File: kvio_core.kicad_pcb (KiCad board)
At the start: 6 copper layers, 60 x 41 mm, 196 parts, among them J1001 16-pin_FFC_(SFV16R), J1101 16-pin_FFC_(SFV16R), J1301 USB3_B_Micro, J401 16-pin_FFC_(SFV16R), J501 16-pin_FFC_(SFV16R), J601 16-pin_FFC_(SFV16R), J701 16-pin_FFC_(SFV16R), J801 16-pin_FFC_(SFV16R), J901 16-pin_FFC_(SFV16R), U1001 EMI8143, U101 XC7A100T-CSG324, U1101 EMI8143, U1201 DDR3-16x, U1301 FT601Q, U1302 EMI8143, U201 FAN53541, U202 FAN53541, U203 FAN53541, U204 FAN53541, U401 EMI8143, U501 EMI8143, U601 EMI8143, U701 EMI8143, U801 EMI8143, U901 EMI8143, Y1301 Crystal_GND24_Small

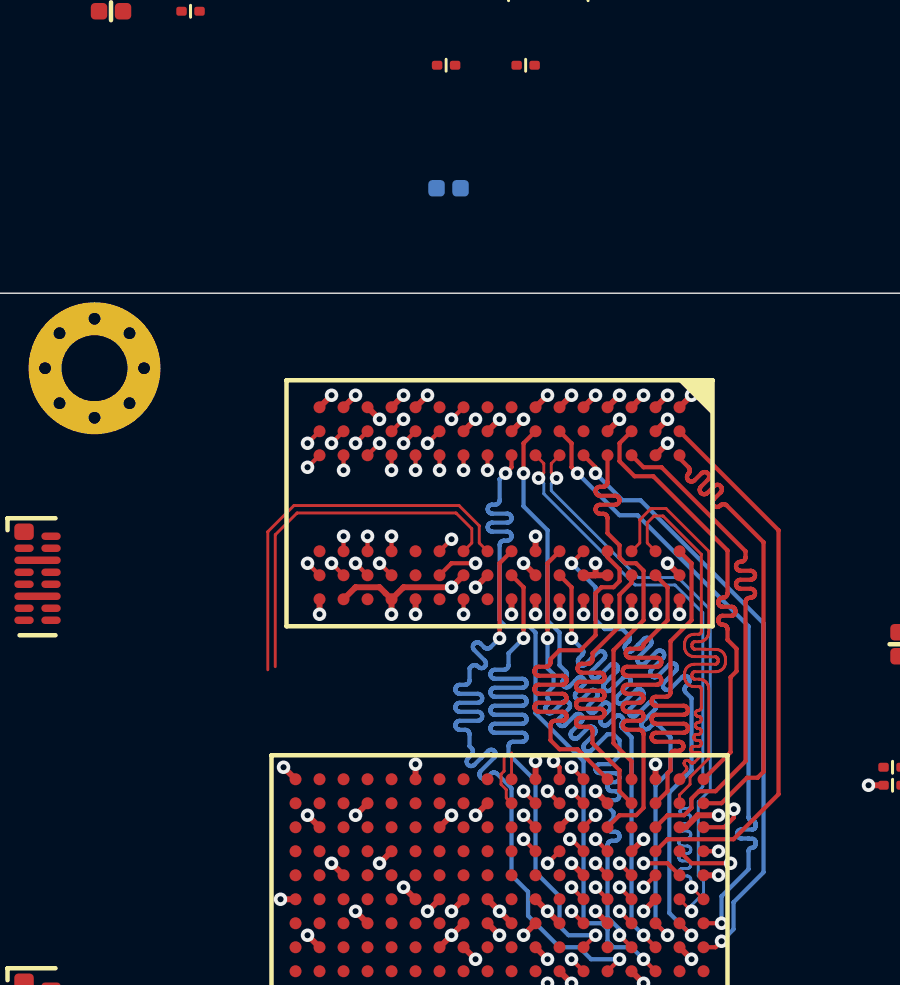
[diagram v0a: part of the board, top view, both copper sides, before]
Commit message: Updates to length matching and added GND plane for DDR3
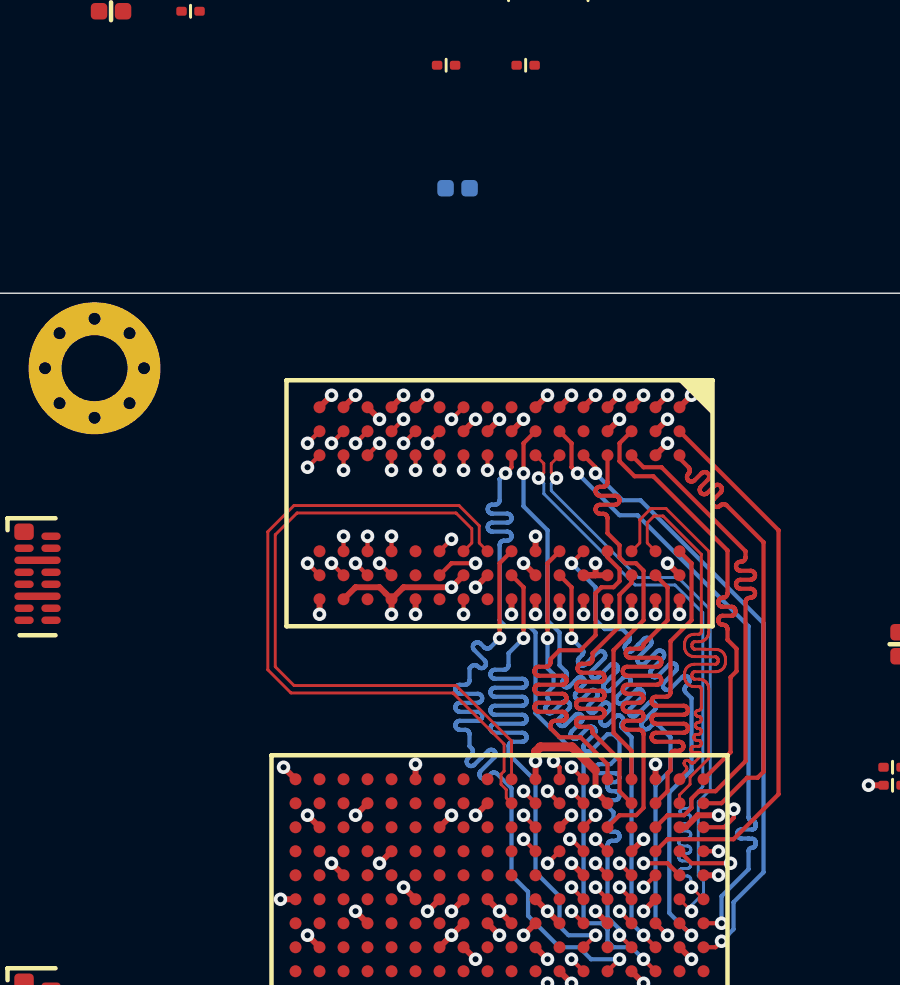
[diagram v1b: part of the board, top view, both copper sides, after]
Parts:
- moved C217 0.30 mm to (183.6, 85.5)
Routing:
- net /DDR Memory/CK_N: track 13.2 -> 22.5 mm
- net /DDR Memory/CK_P: track 15.0 -> 24.3 mm
- net /DDR Memory/DDR3_VDD: track 17.7 -> 21.2 mm
- added copper zone on GND_PWR2, net GND

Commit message: More design
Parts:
- removed C302: 0.1u, passive:C_0201
- added C283: 0.1u, passive:C_0201, F.Cu at (152.0, 111.5)
- added C284: 0.1u, passive:C_0201, F.Cu at (154.2, 111.5)
- added R301: 33, passive:R_0402, F.Cu at (144.4, 111.6)
- added R302: 470, passive:R_0402, F.Cu at (144.4, 113.5)
- added U301: MX25L3233F, Package_SON:WSON-8-1EP_6x5mm_P1.27mm_EP3.4x4.3mm, F.Cu at (139.5, 113.0)
- U101: value XC7A100T-CSG324 -> xc7a100t-csg324
- moved C301 50.6 mm to (141.5, 110.0)
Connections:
- net /VCCO_14 renamed /Power/VCCO_14
- net /VCCO_15 renamed /Power/VCCO_15
- net /VCCO_16 renamed /Power/VCCO_16
- C201 pad 1: /VCCO_34 -> /Power/VCCO_34
- C202 pad 1: /VCCO_35 -> /Power/VCCO_35
- C205 pad 1: /VCCO_34 -> /Power/VCCO_34
- C206 pad 1: /VCCO_35 -> /Power/VCCO_35
- C210 pad 1: /VCCO_34 -> /Power/VCCO_34
- C211 pad 1: /VCCO_35 -> /Power/VCCO_35
- C215 pad 1: /VCCO_34 -> /Power/VCCO_34
- C216 pad 1: /VCCO_35 -> /Power/VCCO_35
- C220 pad 1: /VCCO_34 -> /Power/VCCO_34
- C221 pad 1: /VCCO_35 -> /Power/VCCO_35
- C226 pad 1: /VCCO_34 -> /Power/VCCO_34
- C227 pad 1: /VCCO_35 -> /Power/VCCO_35
- C232 pad 1: /VCCO_34 -> /Power/VCCO_34
- C233 pad 1: /VCCO_35 -> /Power/VCCO_35
- C240 pad 1: /VCCO_34 -> /Power/VCCO_34
- C241 pad 1: /VCCO_35 -> /Power/VCCO_35
- C248 pad 1: /VCCO_34 -> /Power/VCCO_34
- C249 pad 1: /VCCO_35 -> /Power/VCCO_35
- C256 pad 1: /VCCO_34 -> /Power/VCCO_34
- C257 pad 1: /VCCO_35 -> /Power/VCCO_35
- C301 pad 1: /Config/VCCO_0 -> GND
- C301 pad 2: GND -> /Config/3V3
- U101 pad A7: /USB3 Interface/3V3 -> /Power/VCCO_35
- U101 pad C3: /USB3 Interface/3V3 -> /Power/VCCO_35
- U101 pad D6: /USB3 Interface/3V3 -> /Power/VCCO_35
- U101 pad F2: /USB3 Interface/3V3 -> /Power/VCCO_35
- U101 pad G5: /USB3 Interface/3V3 -> /Power/VCCO_35
- U101 pad J1: /USB3 Interface/3V3 -> /Power/VCCO_35
- U101 pad K4: /DDR Memory/DDR3_VDD -> /Power/VCCO_34
- U101 pad N3: /DDR Memory/DDR3_VDD -> /Power/VCCO_34
- U101 pad P6: /DDR Memory/DDR3_VDD -> /Power/VCCO_34
- U101 pad R9: /Config/VCCO_0 -> /Power/VCCO_0
- U101 pad T2: /DDR Memory/DDR3_VDD -> /Power/VCCO_34
- U101 pad U5: /DDR Memory/DDR3_VDD -> /Power/VCCO_34
- U101 pad V8: /DDR Memory/DDR3_VDD -> /Power/VCCO_34
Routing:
- net /Power/VCCO_34: track 0.00 -> 7.84 mm, vias 0 -> 6
- net /DDR Memory/DDR3_VDD: track 21.2 -> 13.3 mm, vias 23 -> 17

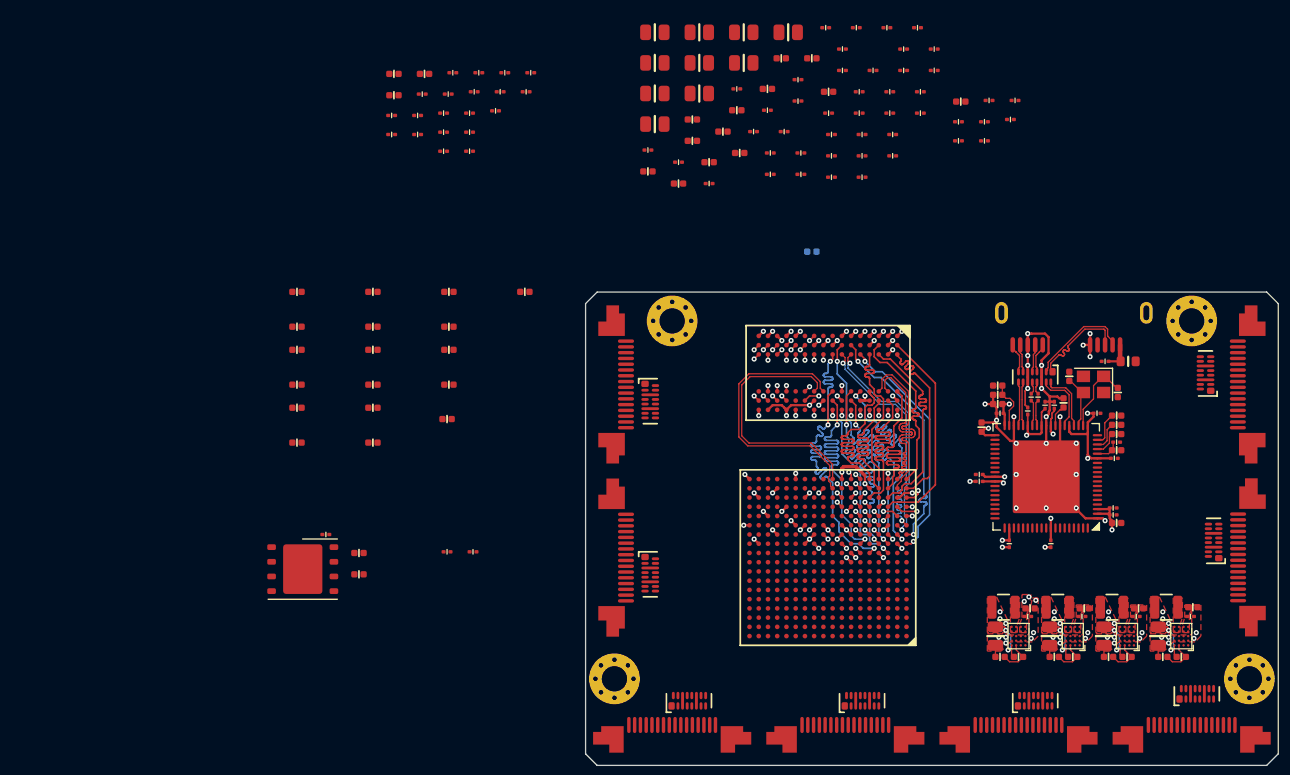
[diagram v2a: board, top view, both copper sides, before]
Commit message: More additions, DDR3 caps placed
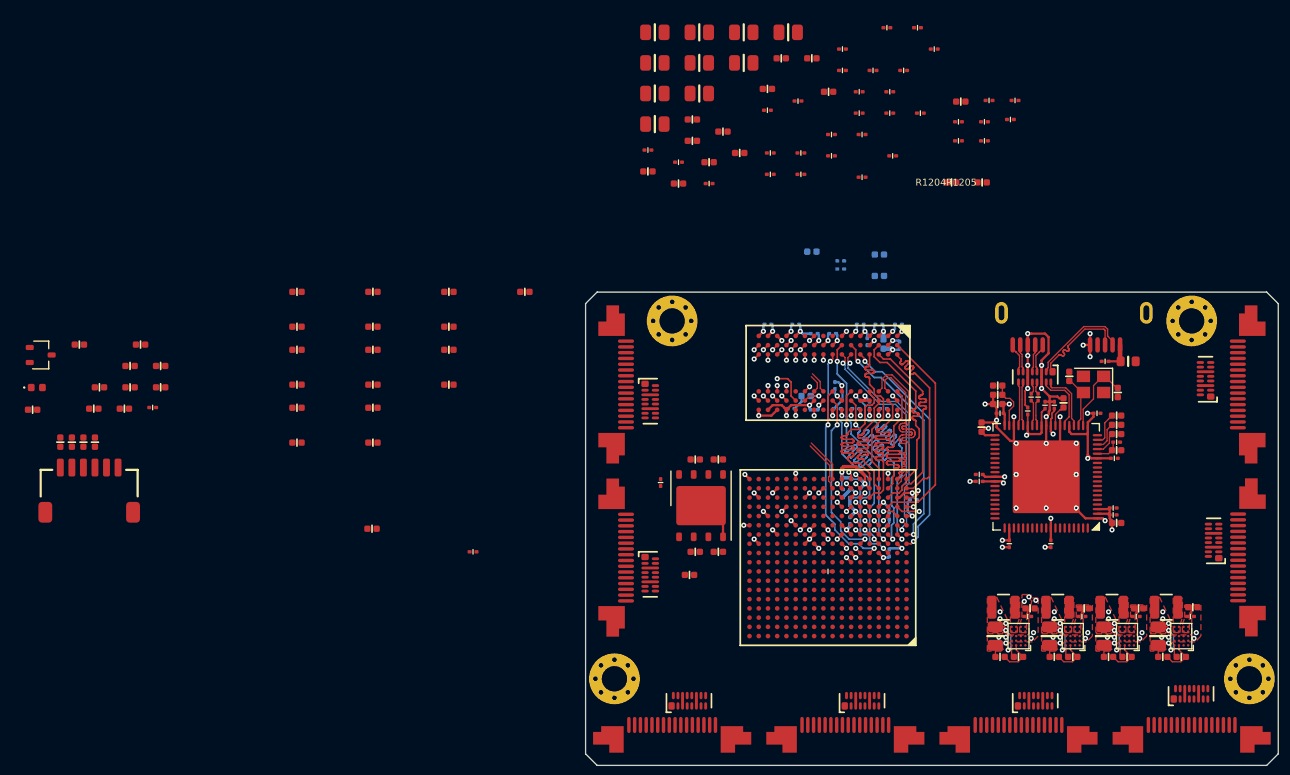
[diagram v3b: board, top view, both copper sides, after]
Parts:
- removed C1205, C1209, C242, C250, C256, C257, C258, C259, C260, C283: 0.1u, passive:C_0201
- removed C222: 4.7u, passive:C_0402
- added C285: 0.1u, passive:C_0201, F.Cu at (185.0, 113.2)
- added C302: 0.1u, passive:C_0201, F.Cu at (126.5, 99.0)
- added D301: GREEN, LED_SMD:LED_0402_1005Metric, F.Cu at (116.5, 97.3)
- added J301: Conn_01x06_Male, connectors:jst-sh-hor-6, F.Cu at (121.0, 106.0)
- added R1204: 80, passive:R_0402, F.Cu at (195.7, 79.5)
- added R1205: 4.7k, passive:R_0402, F.Cu at (198.3, 79.5)
- added R303: 470, passive:R_0402, F.Cu at (127.2, 95.4)
- added R304: 1k, passive:R_0402, F.Cu at (124.0, 99.1)
- added R305: 1k, passive:R_0402, F.Cu at (124.5, 97.2)
- added R306: 1k, passive:R_0402, F.Cu at (124.5, 95.4)
- added R307: 10k, passive:R_0402, F.Cu at (121.4, 99.1)
- added R308: 1k, passive:R_0402, F.Cu at (121.9, 97.2)
- added R309: 1k, passive:R_0402, F.Cu at (127.2, 97.2)
- added R310: 1k, passive:R_0402, F.Cu at (125.5, 93.5)
- added R311: 33, passive:R_0402, F.Cu at (175.5, 103.5)
- added R312: 33, passive:R_0402, F.Cu at (173.5, 111.5)
- added R313: 33, passive:R_0402, F.Cu at (175.5, 111.5)
- added R314: 33, passive:R_0402, F.Cu at (173.5, 103.5)
- added R315: 10k, passive:R_0402, F.Cu at (116.1, 99.2)
- added R316: 10k, passive:R_0402, F.Cu at (120.2, 93.5)
- added R317: 33, passive:R_0402, F.Cu at (118.5, 102.0)
- added R318: 33, passive:R_0402, F.Cu at (119.5, 102.0)
- added R319: 33, passive:R_0402, F.Cu at (120.5, 102.0)
- added R320: 33, passive:R_0402, F.Cu at (121.5, 102.0)
- added U302: MAX809, sot:SOT-323, F.Cu at (116.8, 94.5)
- C1201, C1202, C1203, C1204, C1206, C1207, C1208, C1210, C1211, C1212, C1213, C1214, C1215, C1216, C1217, C1218, C1219, C1220, C1221, C215, C220, C226, C232, C240, C248, R1201, R1202, R1203: moved to B.Cu
- U1201: value DDR3-16x -> MT41J128M16JT-125:K
- moved C1203 46.1 mm to (189.8, 93.5), turned to 270 degrees
- moved C1212 45.8 mm to (191.1, 91.8), turned to 180 degrees
- moved R1202 45.5 mm to (189.4, 87.6)
- moved R1201 44.3 mm to (189.4, 85.8)
- moved C1213 43.6 mm to (191.2, 93.6), turned to 90 degrees
- moved C1204 42.9 mm to (189.4, 91.8), turned to 180 degrees
- moved C215 42.7 mm to (186.9, 108.8), turned to 270 degrees
- moved C220 42.7 mm to (190.3, 108.4), turned to 90 degrees
- moved C1210 42.6 mm to (185.8, 99.1)
- moved C1219 42.4 mm to (189.8, 99.1), turned to 180 degrees
- moved C1214 42.1 mm to (187.4, 99.1), turned to 180 degrees
- moved C1217 41.1 mm to (188.6, 98.8), turned to 270 degrees
- moved C1202 40.9 mm to (186.1, 86.3)
- moved C1206 40.6 mm to (185.4, 92.6), turned to 180 degrees
- moved C1216 40.2 mm to (188.4, 93.3), turned to 90 degrees
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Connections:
- C201 pad 1: /Power/VCCO_34 -> +1V5
- C202 pad 1: /Power/VCCO_35 -> +3V3
- C203 pad 1: /Power/VCCO_15 -> +3V3
- C204 pad 1: /Power/VCCO_14 -> +3V3
- C205 pad 1: /Power/VCCO_34 -> +1V5
- C206 pad 1: /Power/VCCO_35 -> +3V3
- C207 pad 1: /Power/VCCO_15 -> +3V3
- C208 pad 1: /Power/VCCO_14 -> +3V3
- C209 pad 1: /Power/VCCINT -> +1V0
- C210 pad 1: /Power/VCCO_34 -> +1V5
- C211 pad 1: /Power/VCCO_35 -> +3V3
- C212 pad 1: /Power/VCCO_15 -> +3V3
- C213 pad 1: /Power/VCCO_14 -> +3V3
- C214 pad 1: /Power/VCCINT -> +1V0
- C215 pad 1: /Power/VCCO_34 -> +1V5
- C216 pad 1: /Power/VCCO_35 -> +3V3
- C217 pad 1: /Power/VCCO_15 -> +3V3
- C218 pad 1: /Power/VCCO_14 -> +3V3
- C219 pad 1: /Power/VCCINT -> +1V0
- C220 pad 1: /Power/VCCO_34 -> +1V5
- C221 pad 1: /Power/VCCO_35 -> +3V3
- C223 pad 1: /Power/VCCO_15 -> +3V3
- C224 pad 1: /Power/VCCO_14 -> +3V3
- C225 pad 1: /Power/VCCINT -> +1V0
- C226 pad 1: /Power/VCCO_34 -> +1V5
- C227 pad 1: /Power/VCCO_35 -> +3V3
- C228 pad 1: /Power/VCCO_16 -> +3V3
- C229 pad 1: /Power/VCCO_15 -> +3V3
- C230 pad 1: /Power/VCCO_14 -> +3V3
- C231 pad 1: /Power/VCCINT -> +1V0
- C232 pad 1: /Power/VCCO_34 -> +1V5
- C233 pad 1: /Power/VCCO_35 -> +3V3
- C234 pad 1: /Power/VCCO_16 -> +3V3
- C235 pad 1: /Power/VCCO_15 -> +3V3
- C236 pad 1: /Power/VCCO_14 -> +3V3
- C237 pad 1: /Power/VCCINT -> +1V0
- C238 pad 1: /Power/VCCAUX -> +1V8
- C239 pad 1: /Power/VCCBRAM -> +1V0
- C240 pad 1: /Power/VCCO_34 -> +1V5
- C241 pad 1: /Power/VCCO_35 -> +3V3
- C243 pad 1: /Power/VCCO_15 -> +3V3
- C244 pad 1: /Power/VCCO_14 -> +3V3
- C245 pad 1: /Power/VCCINT -> +1V0
- C246 pad 1: /Power/VCCAUX -> +1V8
- C247 pad 1: /Power/VCCAUX -> +1V8
- C248 pad 1: /Power/VCCO_34 -> +1V5
- C249 pad 1: /Power/VCCO_35 -> +3V3
- C251 pad 1: /Power/VCCO_15 -> +3V3
- C252 pad 1: /Power/VCCO_14 -> +3V3
- C253 pad 1: /Power/VCCINT -> +1V0
- C254 pad 1: /Power/VCCAUX -> +1V8
- C255 pad 1: /Power/VCCBRAM -> +1V0
- C261 pad 1: /Power/VCCINT -> +1V0
- C262 pad 1: /Power/VCCAUX -> +1V8
- C263 pad 1: /Power/VCCBRAM -> +1V0
- C264 pad 1: /Power/VCCAUX -> +1V8
- C265 pad 1: /Power/VCCAUX -> +1V8
- C266 pad 1: /Power/VCCINT -> +1V0
- C267 pad 1: /Power/VCCINT -> +1V0
- C268 pad 1: /Power/VCCINT -> +1V0
- C269 pad 1: /Power/VCCINT -> +1V0
- C270 pad 1: /Power/VCCINT -> +1V0
- C273 pad 1: /Power/3V3 -> +3V3
- C276 pad 1: /Power/1V8 -> +1V8
- C279 pad 1: /Power/1V35 -> +1V5
- C282 pad 1: /Power/1V0 -> +1V0
- C284 pad 1: /Power/VCCO_0 -> +3V3
- FB201 pad 1: Net-(FB201-Pad1) -> /Power/VCCADC
- FB201 pad 2: Net-(FB201-Pad2) -> +1V8
- L201 pad 2: /Power/3V3 -> +3V3
- L202 pad 2: /Power/1V8 -> +1V8
- L203 pad 2: /Power/1V35 -> +1V5
- L204 pad 2: /Power/1V0 -> +1V0
- R201 pad 1: /Power/3V3 -> +3V3
- R203 pad 1: /Power/1V8 -> +1V8
- R205 pad 1: /Power/1V35 -> +1V5
- R207 pad 1: /Power/1V0 -> +1V0
- R301 pad 1: Net-(R301-Pad1) -> /Config/CFG_CLK
- R302 pad 1: Net-(D301-Pad2) -> /Config/CFG_DONE
- U101 pad A17: /Power/VCCO_15 -> +3V3
- U101 pad A7: /Power/VCCO_35 -> +3V3
- U101 pad B10: /Power/VCCO_16 -> +3V3
- U101 pad C13: /Power/VCCO_15 -> +3V3
- U101 pad C3: /Power/VCCO_35 -> +3V3
- U101 pad D16: /Power/VCCO_15 -> +3V3
- U101 pad D6: /Power/VCCO_35 -> +3V3
- U101 pad E10: Net-(U101-PadE10) -> /Config/TCK
- U101 pad E11: Net-(U101-PadE11) -> /Config/TDI
- U101 pad E12: Net-(U101-PadE12) -> /Config/TMS
- U101 pad E13: Net-(U101-PadE13) -> /Config/TDO
- U101 pad E8: /Power/VCCBAT -> +1V8
- U101 pad E9: Net-(U101-PadE9) -> Net-(R301-Pad2)
- U101 pad F10: /Power/VCCBRAM -> +1V0
- U101 pad F12: /Power/VCCAUX -> +1V8
- U101 pad F2: /Power/VCCO_35 -> +3V3
- U101 pad F8: /Power/VCCINT -> +1V0
- U101 pad G11: /Power/VCCBRAM -> +1V0
- U101 pad G15: /Power/VCCO_15 -> +3V3
- U101 pad G5: /Power/VCCO_35 -> +3V3
- U101 pad G7: /Power/VCCINT -> +1V0
- U101 pad G9: /Power/VCCINT -> +1V0
- U101 pad H12: /Power/VCCAUX -> +1V8
- U101 pad H18: /Power/VCCO_15 -> +3V3
- U101 pad H8: /Power/VCCINT -> +1V0
- U101 pad H9: /Power/GNDADC -> GND
- U101 pad J1: /Power/VCCO_35 -> +3V3
- U101 pad J10: Net-(U101-PadJ10) -> GND
- U101 pad J11: /Power/VCCINT -> +1V0
- U101 pad J7: /Power/VCCINT -> +1V0
- U101 pad J9: Net-(U101-PadJ9) -> GND
- U101 pad K10: Net-(U101-PadK10) -> GND
- U101 pad K12: /Power/VCCAUX -> +1V8
- U101 pad K14: /Power/VCCO_15 -> +3V3
- U101 pad K17: Net-(U101-PadK17) -> /Config/CFG_D0
- U101 pad K18: Net-(U101-PadK18) -> /Config/CFG_D1
- U101 pad K4: /Power/VCCO_34 -> +1V5
- U101 pad K8: /Power/VCCINT -> +1V0
- U101 pad K9: Net-(U101-PadK9) -> GND
- U101 pad L10: Net-(U101-PadL10) -> GND
- U101 pad L11: /Power/VCCINT -> +1V0
- U101 pad L13: Net-(U101-PadL13) -> /Config/CFG_CS
- U101 pad L14: Net-(U101-PadL14) -> /Config/CFG_D2
- U101 pad L15: Net-(U101-PadL15) -> /Config/CFG_PUDC
- U101 pad L17: /Power/VCCO_14 -> +3V3
- U101 pad L7: /Power/VCCINT -> +1V0
- U101 pad L9: Net-(U101-PadL9) -> GND
- U101 pad M10: /Power/VCCINT -> +1V0
- U101 pad M12: /Power/VCCAUX -> +1V8
- U101 pad M14: Net-(U101-PadM14) -> /Config/CFG_D3
- U101 pad M8: /Power/VCCINT -> +1V0
- U101 pad N11: /Power/VCCINT -> +1V0
- U101 pad N13: /Power/VCCO_14 -> +3V3
- U101 pad N3: /Power/VCCO_34 -> +1V5
- U101 pad N7: /Power/VCCINT -> +1V0
- U101 pad N9: /Power/VCCINT -> +1V0
- U101 pad P10: Net-(U101-PadP10) -> /Config/CFG_DONE
- U101 pad P11: Net-(U101-PadP11) -> /Config/CFG_MODE2
- U101 pad P12: Net-(U101-PadP12) -> /Config/CFG_MODE0
- U101 pad P13: Net-(U101-PadP13) -> /Config/CFG_MODE1
- U101 pad P16: /Power/VCCO_14 -> +3V3
- U101 pad P6: /Power/VCCO_34 -> +1V5
- U101 pad P7: Net-(U101-PadP7) -> /Config/CFG_INIT_B
- U101 pad P8: Net-(U101-PadP8) -> /Config/3V3
- U101 pad P9: Net-(U101-PadP9) -> /Config/CFG_PROGRAM_B
- U101 pad R9: /Power/VCCO_0 -> +3V3
- U101 pad T12: /Power/VCCO_14 -> +3V3
- U101 pad T2: /Power/VCCO_34 -> +1V5
- U101 pad U15: /Power/VCCO_14 -> +3V3
- U101 pad U5: /Power/VCCO_34 -> +1V5
- U101 pad V18: /Power/VCCO_14 -> +3V3
- U101 pad V8: /Power/VCCO_34 -> +1V5
- U201 pad A4: /Power/3V3 -> +3V3
- U202 pad A4: /Power/1V8 -> +1V8
- U203 pad A4: /Power/1V35 -> +1V5
- U204 pad A4: /Power/1V0 -> +1V0
- U301 pad 1: Net-(U301-Pad1) -> /Config/CFG_CS
- U301 pad 6: Net-(U301-Pad6) -> /Config/CFG_CLK
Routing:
- net GND: track 72.2 -> 97.4 mm
- net +1V5: track 0.00 -> 22.4 mm, vias 0 -> 11
- net /DDR Memory/CK_P: track 24.3 -> 6.49 mm
- net /DDR Memory/CK_N: track 22.5 -> 5.50 mm
- net /DDR Memory/DDR3_VDD: track 13.3 -> 26.5 mm
- net /DDR Memory/DQ5: track 23.2 -> 15.0 mm
- net +3V3: track 0.00 -> 7.87 mm, vias 0 -> 11
- net /Power/VCCO_34: track 7.84 -> 0.00 mm, vias 6 -> 0
- net /DDR Memory/DQ7: track 25.0 -> 17.2 mm
- net /DDR Memory/A1: track 21.8 -> 14.4 mm
- net +1V0: track 0.00 -> 7.31 mm, vias 0 -> 10
- net /DDR Memory/LDQS_N: track 21.3 -> 15.4 mm
- net /Power/3V3: track 4.48 -> 0.00 mm, vias 5 -> 0
- net /Power/1V8: track 4.48 -> 0.00 mm, vias 5 -> 0
- net +1V8: track 0.00 -> 4.48 mm, vias 0 -> 5
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- added copper zone on F.Cu, net +1V0
- added copper zone on F.Cu, net +1V5
- added copper zone on F.Cu, net +1V8
- added copper zone on F.Cu, net +3V3
- removed copper zone on F.Cu, net /Power/1V0
- removed copper zone on F.Cu, net /Power/1V35
- removed copper zone on F.Cu, net /Power/1V8
- removed copper zone on F.Cu, net /Power/3V3
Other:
- net class Default: clearance 0.1 -> 0.0889
- net class power: clearance 0.1 -> 0.0889
- rule trace_clearance: 0.1 -> 0.0889

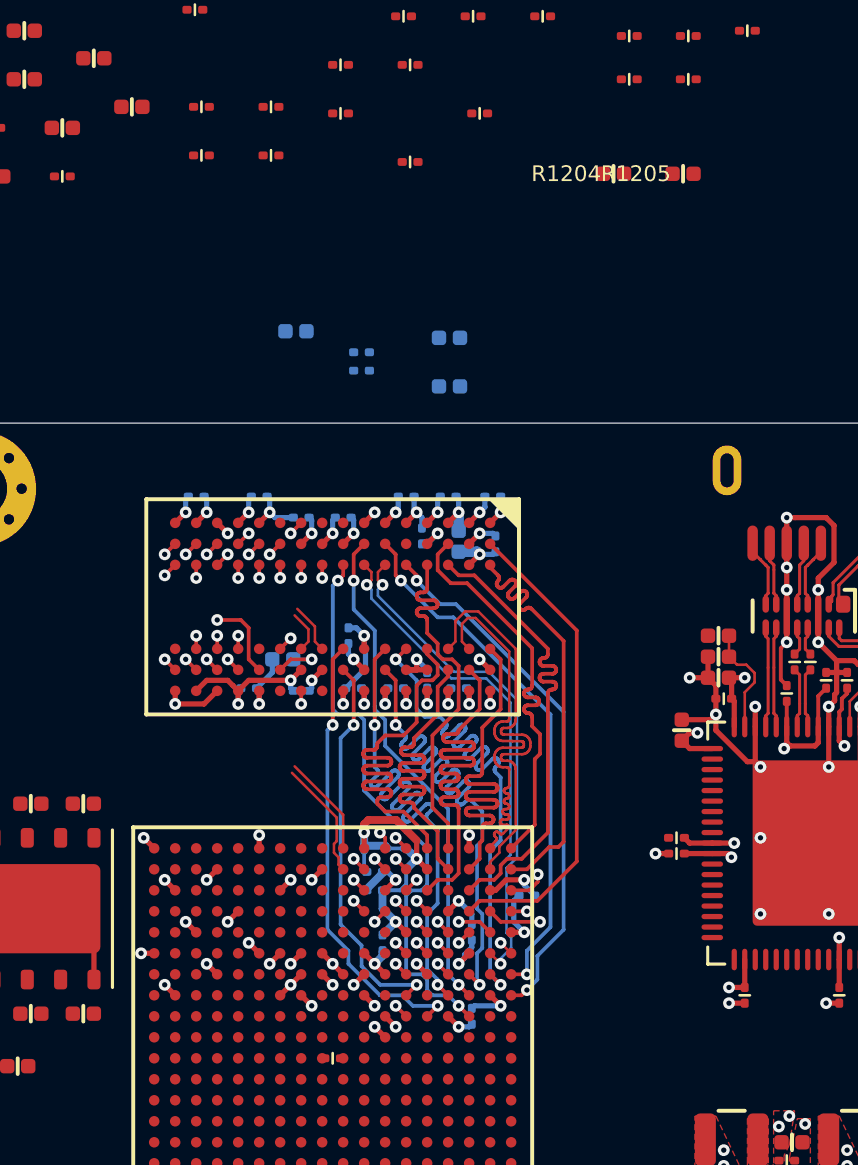
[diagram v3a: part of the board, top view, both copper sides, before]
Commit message: Fixing with DDR3, needs retuning
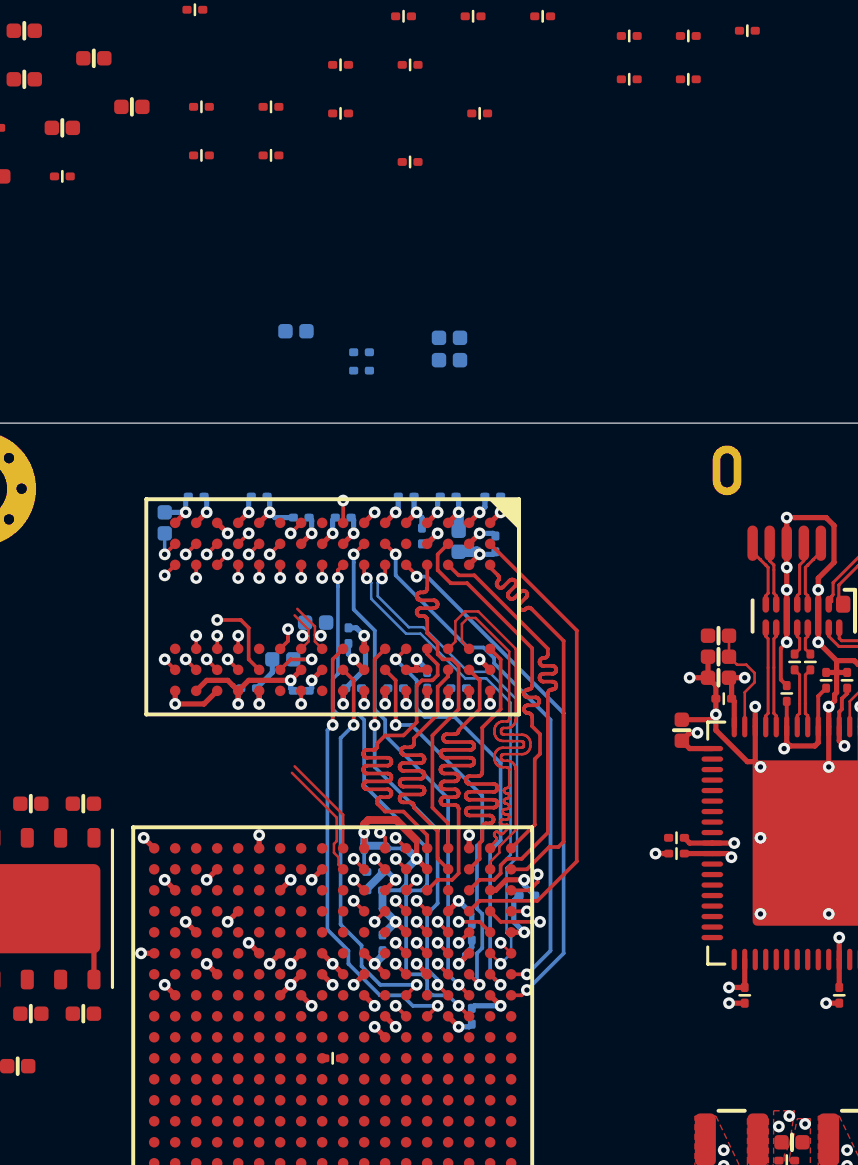
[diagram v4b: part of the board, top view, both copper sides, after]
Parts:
- R1204, R1205: moved to B.Cu
- moved R1205 23.8 mm to (178.6, 92.8), turned to 90 degrees
- moved R1204 20.5 mm to (184.3, 96.6), turned to 180 degrees
- moved R1202 1.00 mm to (189.4, 86.6)
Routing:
- net /DDR Memory/DQ1: track 22.8 -> 14.9 mm
- net /DDR Memory/DQ3: track 22.4 -> 14.7 mm
- net /DDR Memory/A10: track 25.4 -> 19.6 mm
- net /DDR Memory/LDM: track 21.4 -> 16.2 mm
- net /DDR Memory/BA1: track 23.8 -> 18.6 mm
- net /DDR Memory/RAS_N: track 24.8 -> 21.6 mm
- net /DDR Memory/BA2: track 25.7 -> 23.2 mm
- net /DDR Memory/A8: track 20.3 -> 18.3 mm
- net /DDR Memory/VREF: track 3.09 -> 3.94 mm, vias 1 -> 2
- net GND: track 97.4 -> 98.2 mm
- net /DDR Memory/RESET_N: track 26.2 -> 27.0 mm
- net /DDR Memory/WE_N: track 28.6 -> 27.9 mm
- net /DDR Memory/CK_P: track 6.49 -> 6.72 mm, vias 0 -> 1
- net /DDR Memory/CK_N: track 5.50 -> 5.73 mm, vias 0 -> 1
